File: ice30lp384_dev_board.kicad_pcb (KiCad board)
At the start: 2 copper layers, 12.7 x 21.3 mm, 15 parts, among them J1 Conn_01x08, J2 Conn_01x08, U1 MIC5365-1.2YC5-TR, U2 ECS-TXO-2520-33-250-AN-TR, U3 ICE40LP384-SG32, U4 W25X10CLSNIG

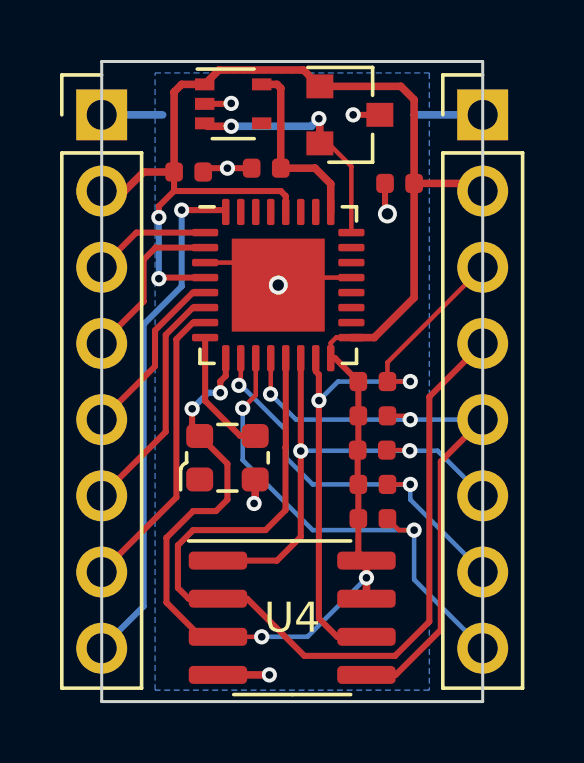
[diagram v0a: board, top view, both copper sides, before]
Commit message: Removed ground connection from 2.5V Diode
Updated files to change ground connection to no-connection for 2.5v diode. v1.0 boards have cut traces to prevent short to ground.
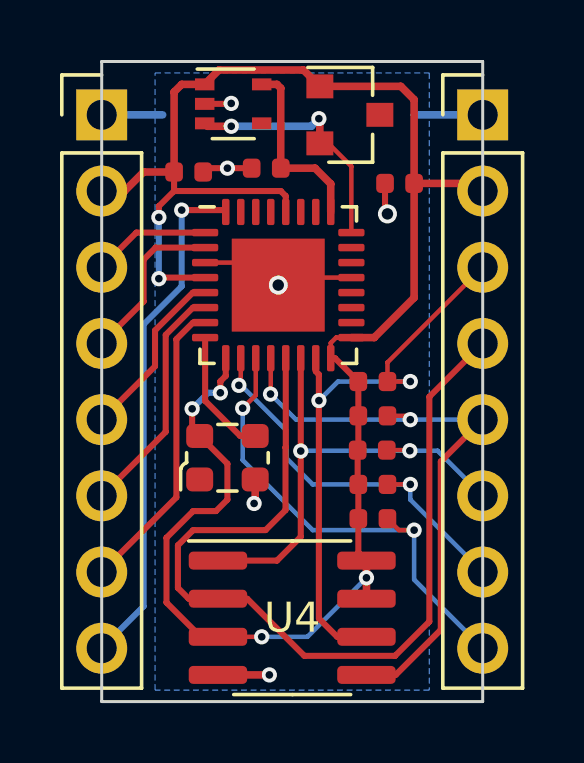
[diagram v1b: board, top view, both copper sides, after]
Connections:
- D1 pad 3: GND -> (no net)
- U1 pad 4: Net-(U1-Pad4) -> (no net)
- U2 pad 1: Net-(U2-Pad1) -> (no net)
- U3 pad 18: Net-(U3-Pad18) -> (no net)
- U3 pad 19: Net-(U3-Pad19) -> (no net)
- U3 pad 20: Net-(U3-Pad20) -> (no net)
- U3 pad 22: Net-(U3-Pad22) -> (no net)
- U3 pad 23: Net-(U3-Pad23) -> (no net)
- U3 pad 26: Net-(U3-Pad26) -> (no net)
- U3 pad 27: Net-(U3-Pad27) -> (no net)
- U3 pad 29: Net-(U3-Pad29) -> (no net)
- U3 pad 30: Net-(U3-Pad30) -> (no net)
- U3 pad 31: Net-(U3-Pad31) -> (no net)
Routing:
- net GND: track 16.6 -> 15.7 mm, vias 7 -> 6
